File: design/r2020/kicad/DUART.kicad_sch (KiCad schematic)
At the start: 17 parts, among them IC4 XR68C681CJTR-F, J1 UART_A, J2 UART_B, J4 Conn_01x06, J7 Conn_01x01_Male, Q1 3.6864MHz

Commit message: Complete Kicad 7 migration
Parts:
- J1, J2: symbol Connector:Conn_01x06_Male -> Connector:Conn_01x06_Pin
- J7: symbol Connector:Conn_01x01_Male -> Connector:Conn_01x01_Pin
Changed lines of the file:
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@@
     )
   )
-  (symbol (lib_id "Connector:Conn_01x06_Male") (at 31.75 148.59 0) (unit 1)
+  (symbol (lib_id "Connector:Conn_01x06_Pin") (at 31.75 148.59 0) (unit 1)
     (in_bom yes) (on_board yes) (dnp no)
     (property "Reference" "J1" (at 34.4932 138.9126 0)
@@
     )
   )
-  (symbol (lib_id "Connector:Conn_01x06_Male") (at 31.75 170.18 0) (unit 1)
+  (symbol (lib_id "Connector:Conn_01x06_Pin") (at 31.75 170.18 0) (unit 1)
     (in_bom yes) (on_board yes) (dnp no)
     (property "Reference" "J2" (at 34.4932 160.5026 0)
@@
     )
   )
-  (symbol (lib_id "Connector:Conn_01x01_Male") (at 101.6 143.51 180) (unit 1)
+  (symbol (lib_id "Connector:Conn_01x01_Pin") (at 101.6 143.51 180) (unit 1)
     (in_bom yes) (on_board yes) (dnp no)
     (property "Reference" "J7" (at 99.06 139.7 0)

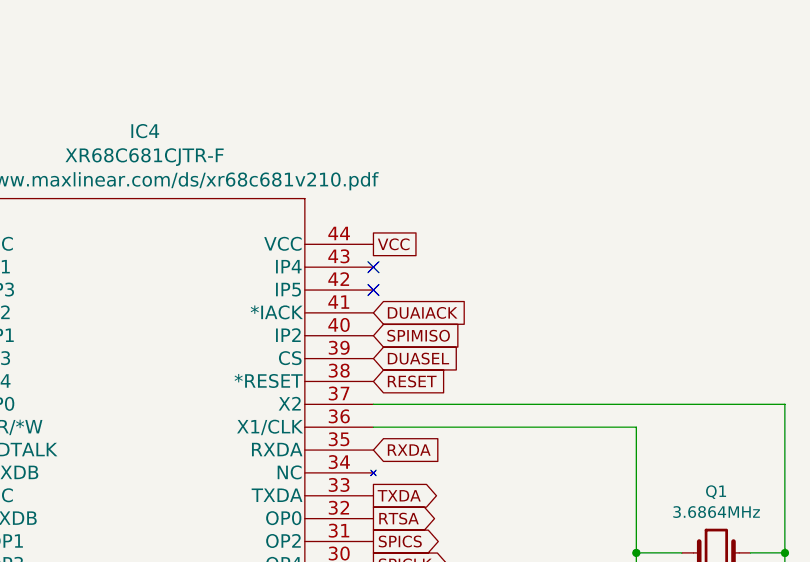
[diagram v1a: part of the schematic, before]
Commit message: Feature/swap tx rx again (#395)
* Swap TX/RX & CTS/RTS silkscreen r2

* Swap over labels
* Add arrows
* Some board tidy up

* Swap TX/RX & CTS/RTS silkscreen r2020

    * Swap over labels
    * Add arrows
    * Some board tidy up
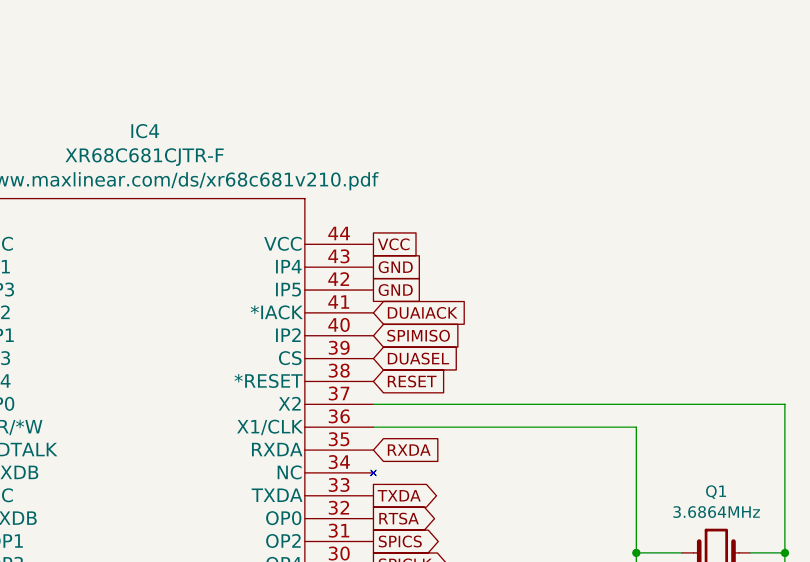
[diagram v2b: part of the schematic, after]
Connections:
- net GND: now also IC4.42 (IP5), IC4.43 (IP4)
- no-connect marks 2 -> 0
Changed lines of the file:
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@@
   (title_block
     (title "ROSCO_M68K CLASSIC MC68020 EDITION")
-    (date "2022-03-30")
+    (date "2023-12-10")
     (rev "1.0")
     (company "The Really Old-School Company Limited")
@@
     (comment 2 "See https://github.com/roscopeco/rosco_m68k/blob/master/LICENCE.hardware.txt")
     (comment 3 "Open Source Hardware licenced under CERN Open Hardware Licence")
-    (comment 4 "Copyright 2019-2022 Ross Bamford and Contributors")
+    (comment 4 "Copyright 2019-2023 Ross Bamford and Contributors")
   )
   (junction (at 38.1 48.26) (diameter 0) (color 0 0 0 0)
@@
   (junction (at 191.77 80.01) (diameter 0) (color 0 0 0 0)
   )
-  (no_connect (at 162.56 50.8))
-  (no_connect (at 162.56 48.26))
   (wire (pts (xy 92.71 52.07) (xy 86.36 52.07))
     (stroke (width 0) (type default))
@@
     )
   )
+  (global_label "GND" (shape passive) (at 162.56 48.26 0) (fields_autoplaced)
+    (effects (font (size 1.27 1.27)) (justify left))
+    (property "Intersheetrefs" "${INTERSHEET_REFS}" (at 167.809 48.26 0)
+      (effects (font (size 1.27 1.27)) (justify left) hide)
+    )
+  )
   (global_label "D4" (shape bidirectional) (at 162.56 91.44 0) (fields_autoplaced)
     (effects (font (size 1.27 1.27)) (justify left))
@@
     )
   )
+  (global_label "GND" (shape passive) (at 162.56 50.8 0) (fields_autoplaced)
+    (effects (font (size 1.27 1.27)) (justify left))
+    (property "Intersheetrefs" "${INTERSHEET_REFS}" (at 167.809 50.8 0)
+      (effects (font (size 1.27 1.27)) (justify left) hide)
+    )
+  )
